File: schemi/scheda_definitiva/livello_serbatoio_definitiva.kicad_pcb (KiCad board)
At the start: 2 copper layers, 83 x 72 mm, 36 parts, among them J1 USB_B, J2 CONN_US, J3 CONN_LCD, J4 BTN_LED_GROUP, J5 ICSP, SW1 SW_RST, U1 FT232RL, U2 ATmega328P-PU, Y1 16MHz

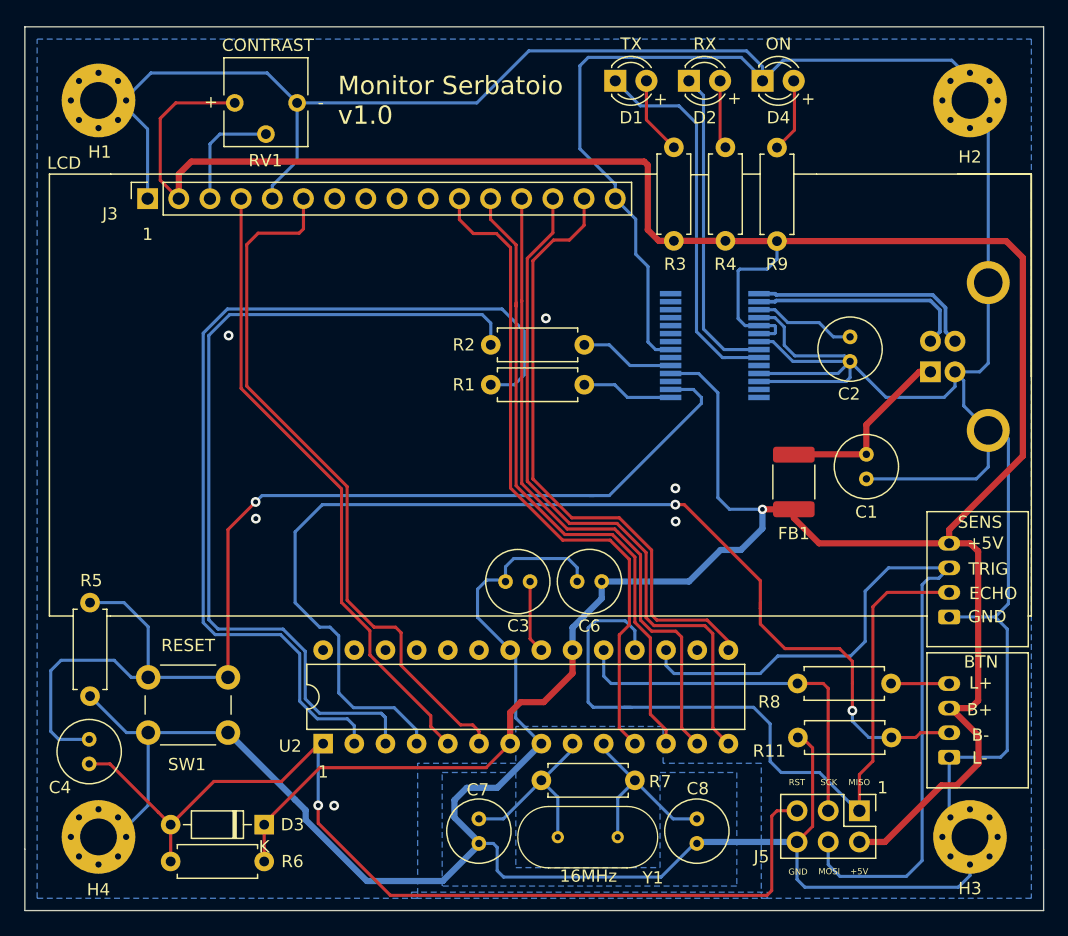
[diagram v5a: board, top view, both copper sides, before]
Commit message: fix a scheda - corrette footprint (adeguate a componenti in possesso) - nuovo routing e layout scheda - aggiunto logo - aggiornato gerber
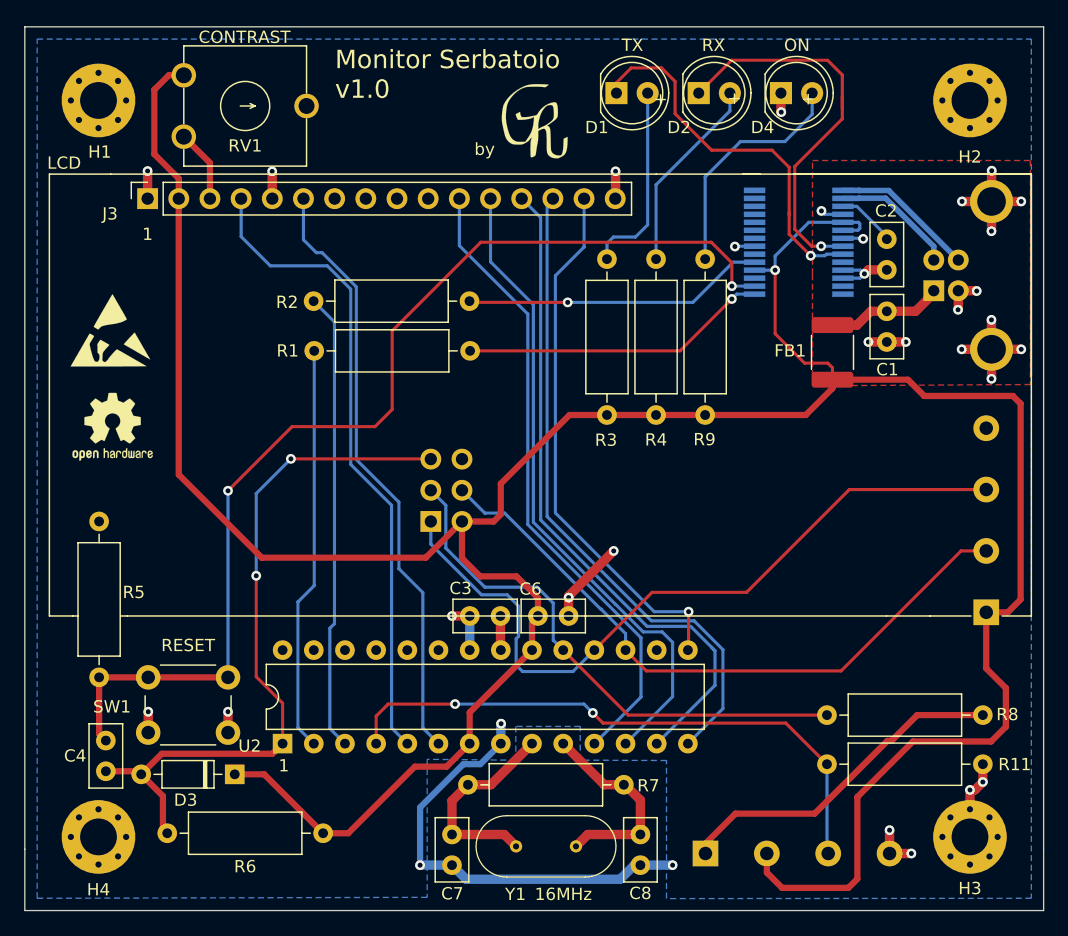
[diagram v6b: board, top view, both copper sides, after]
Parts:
- added G***: LOGO, simboli_custom:logo, F.Cu at (128.5, 75.7)
- added REF**: OSHW-Logo2_7.3x6mm_SilkScreen, Symbol:OSHW-Logo2_7.3x6mm_SilkScreen, F.Cu at (94.2, 100.6)
- added REF**: ESD-Logo_6.6x6mm_SilkScreen, Symbol:ESD-Logo_6.6x6mm_SilkScreen, F.Cu at (94.0, 92.7)
- C1, C2, C3, C4, C6, C7, C8: footprint Capacitor_THT:C_Radial_D5.0mm_H5.0mm_P2.00mm -> Capacitor_THT:C_Disc_D5.0mm_W2.5mm_P2.50mm
- D1, D2, D4: footprint LED_THT:LED_D3.0mm -> LED_THT:LED_D5.0mm
- J2: value CONN_US -> BTN_LED_GROUP; footprint Connector_Molex:Molex_Micro-Latch_53254-0470_1x04_P2.00mm_Horizontal -> simboli_custom:TerminalBlock_RND_205-00047_1x04_P5.00mm_Horizontal
- J4: value BTN_LED_GROUP -> CONN_US; footprint Connector_Molex:Molex_Micro-Latch_53254-0470_1x04_P2.00mm_Horizontal -> simboli_custom:TerminalBlock_RND_205-00047_1x04_P5.00mm_Horizontal
- J5: moved to B.Cu
- R1, R11, R2, R3, R4, R5, R6, R7, R9: footprint Resistor_THT:R_Axial_DIN0207_L6.3mm_D2.5mm_P7.62mm_Horizontal -> Resistor_THT:R_Axial_DIN0309_L9.0mm_D3.2mm_P12.70mm_Horizontal
- R8: value 390 -> 330; footprint Resistor_THT:R_Axial_DIN0207_L6.3mm_D2.5mm_P7.62mm_Horizontal -> Resistor_THT:R_Axial_DIN0309_L9.0mm_D3.2mm_P12.70mm_Horizontal
- RV1: footprint Potentiometer_THT:Potentiometer_Vishay_T73YP_Vertical -> simboli_custom:Trimmer_ACP_470
- SW1: footprint Button_Switch_THT:SW_PUSH_6mm -> Button_Switch_THT:SW_PUSH_6mm_H5mm
- moved J5 42.1 mm to (120.1, 108.3), turned to 0 degrees
- moved J2 27.7 mm to (142.4, 135.3), turned to 0 degrees
- moved R4 15.3 mm to (138.4, 99.6)
- moved R3 15.2 mm to (134.4, 99.6)
- moved R2 14.9 mm to (110.5, 90.3)
- moved R1 14.6 mm to (110.6, 94.4)
- moved J4 12.2 mm to (165.3, 115.7)
- moved C1 11.8 mm to (157.2, 91.2)
- moved FB1 11.0 mm to (152.8, 94.5)
- moved U1 10.8 mm to (150.1, 85.5)
- moved R9 10.8 mm to (142.4, 86.9)
- moved C2 8.50 mm to (157.2, 85.3)
- moved J1 6.62 mm to (161.1, 89.5)
- moved R5 6.13 mm to (93.0, 121.0), turned to 90 degrees
- moved R7 5.99 mm to (123.1, 129.8)
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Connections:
- C1 pad 2: BLK -> GND
- C2 pad 2: BLK -> GND
- C3 pad 2: BLK -> GND
- C6 pad 2: BLK -> GND
- C7 pad 1: BLK -> GND
- C8 pad 1: BLK -> GND
- D4 pad 1: BLK -> GND
- H1 pad 1: BLK -> GND
- H2 pad 1: BLK -> GND
- H3 pad 1: BLK -> GND
- H4 pad 1: BLK -> GND
- J1 pad 4: BLK -> GND
- J1 pad 5: BLK -> GND
- J2 pad 1: BLK -> Net-(J2-Pad1)
- J2 pad 2: D12 -> VDD
- J2 pad 3: D11 -> D2
- J2 pad 4: VDD -> GND
- J3 pad 1: BLK -> GND
- J3 pad 16: BLK -> GND
- J3 pad 5: BLK -> GND
- J4 pad 1: BLK -> VDD
- J4 pad 2: D2 -> D11
- J4 pad 3: VDD -> D12
- J4 pad 4: Net-(J4-Pad4) -> GND
- J5 pad 6: BLK -> GND
- R11 pad 2: BLK -> GND
- R5 pad 2: BLK -> GND
- R8 pad 2: Net-(J4-Pad4) -> Net-(J2-Pad1)
- RV1 pad 3: BLK -> GND
- SW1 pad 2: BLK -> GND
- U1 pad 18: BLK -> GND
- U1 pad 21: BLK -> GND
- U1 pad 25: BLK -> GND
- U1 pad 26: BLK -> GND
- U1 pad 7: BLK -> GND
- U2 pad 22: BLK -> GND
- U2 pad 8: BLK -> GND
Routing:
- net BLK: track 425.6 -> 0.00 mm, vias 6 -> 0
- net GND: track 0.00 -> 106.1 mm, vias 0 -> 32
- net TX: track 77.4 -> 33.1 mm
- net D2: track 91.4 -> 48.9 mm
- net RX: track 71.5 -> 37.4 mm
- net Net-(J2-Pad1): track 0.00 -> 27.7 mm
- net ICSP_RST: track 81.3 -> 57.9 mm, vias 1 -> 2
- net Net-(R1-Pad2): track 7.46 -> 25.1 mm, vias 0 -> 1
- net Net-(R2-Pad2): track 7.73 -> 24.6 mm, vias 0 -> 1
- net Net-(D4-Pad2): track 6.05 -> 19.3 mm
- net D13: track 30.8 -> 43.7 mm
- net D11: track 66.2 -> 53.6 mm
- net VDD: track 260.1 -> 248.8 mm
- net Net-(D2-Pad2): track 5.60 -> 16.0 mm
- net Net-(D1-Pad2): track 6.34 -> 16.0 mm
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- added copper zone on B.Cu, net GND
- added copper zone on F.Cu, net GND
- removed copper zone on B.Cu, net BLK
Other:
- board text added: "E"
- board text added: "T"
- board text added: "W: 17.7 mils / D: 7 mils / PCB thickness: 0.6 mm 2-layer FR-4 Zdiff: 102ohm (in range 90ohm +-15%) Zcomm: 52.5 ohm (leggermente fuori range 45ohm +- 15%)"
- board text added: "by"
- board text removed: "-"
- board text removed: "ECHO"
- board text removed: "TRIG"

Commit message: aggiunta protezione ESD - nuovo routing usb - nuove immagini pcb
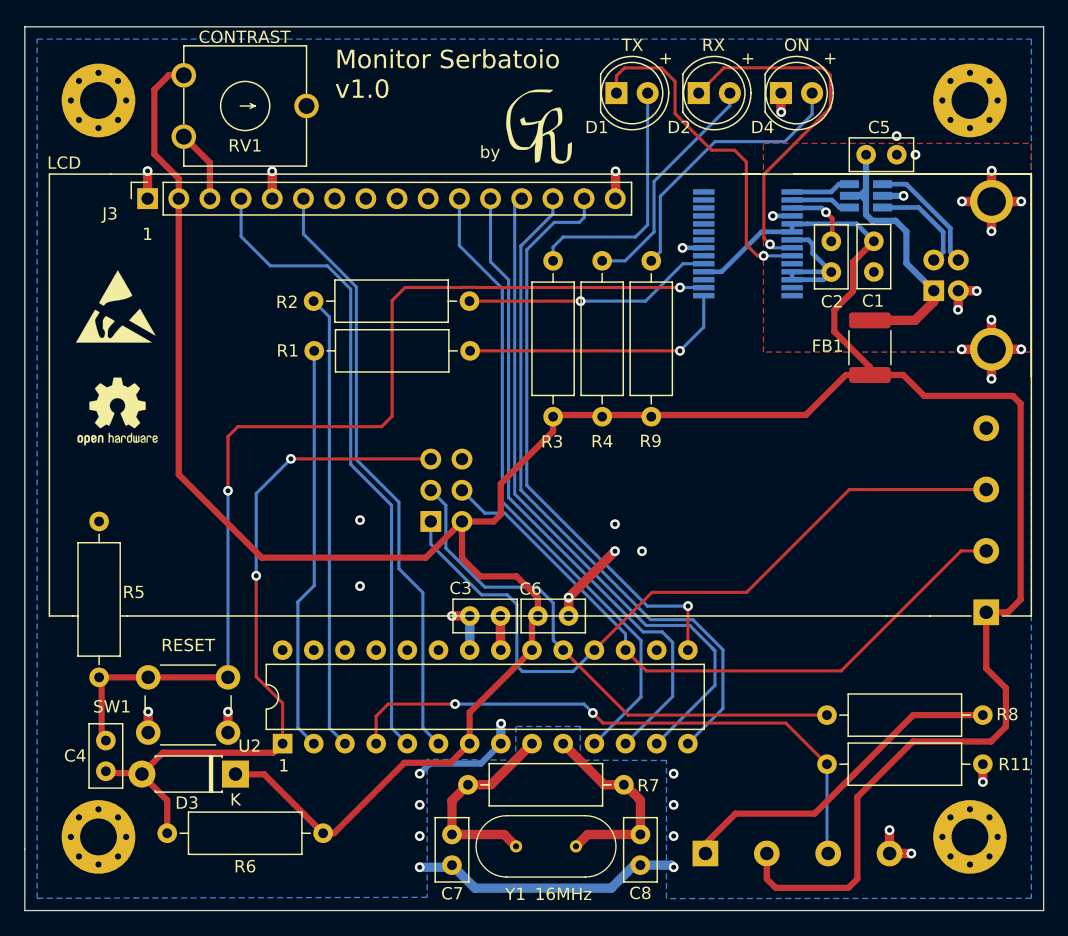
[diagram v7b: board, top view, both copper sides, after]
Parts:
- added C5: 100nF, Capacitor_THT:C_Disc_D5.0mm_W2.5mm_P2.50mm, F.Cu at (158.0, 78.4)
- added U3: USBLC6-2SC6, Package_TO_SOT_SMD:SOT-23-6_Handsoldering, B.Cu at (155.5, 81.8)
- D3: value 1N4148TR -> 1N4700; footprint Diode_THT:D_DO-35_SOD27_P7.62mm_Horizontal -> Diode_THT:D_DO-41_SOD81_P7.62mm_Horizontal
- moved C2 4.53 mm to (152.7, 85.5)
- moved R3 4.39 mm to (130.0, 99.8)
- moved R4 4.39 mm to (134.0, 99.8)
- moved R9 4.39 mm to (138.0, 87.1)
- moved U1 4.14 mm to (145.9, 85.7)
- moved C1 3.37 mm to (156.2, 88.0), turned to 90 degrees
- moved FB1 3.07 mm to (155.8, 94.1)
- moved REF** 1.99 mm to (94.4, 90.8)
- moved REF** 1.31 mm to (94.5, 99.3)
- moved G*** 0.56 mm to (128.9, 76.1)
- moved D3 0.06 mm to (104.2, 128.9)
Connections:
- C1 pad 1: Net-(C1-Pad1) -> GND
- C1 pad 2: GND -> VDD
- FB1 pad 2: Net-(C1-Pad1) -> VBUS
- J1 pad 1: Net-(C1-Pad1) -> VBUS
- J1 pad 2: /D- -> D_IN_-
- J1 pad 3: /D+ -> D_IN_+
- U1 pad 15: /D+ -> D_OUT_+
- U1 pad 16: /D- -> D_OUT_-
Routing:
- net VBUS: track 0.00 -> 23.3 mm
- net /D+: track 11.8 -> 0.00 mm
- net /D-: track 10.1 -> 0.00 mm
- net D_IN_+: track 0.00 -> 9.87 mm
- net Net-(C1-Pad1): track 9.53 -> 0.00 mm
- net D_IN_-: track 0.00 -> 8.44 mm
- net VDD: track 248.8 -> 256.0 mm, vias 1 -> 0
- net GND: track 106.1 -> 99.1 mm, vias 32 -> 40
- net D_OUT_+: track 0.00 -> 4.93 mm
- net D_OUT_-: track 0.00 -> 4.92 mm
- net Net-(D1-Pad2): track 16.0 -> 20.3 mm
- net Net-(R2-Pad2): track 24.6 -> 20.3 mm
- net DTR: track 88.7 -> 84.8 mm
- net BLA: track 43.9 -> 47.3 mm
- net Net-(D1-Pad1): track 31.1 -> 27.8 mm
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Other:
- board text removed: "W: 17.7 mils / D: 7 mils / PCB thickness: 0.6 mm 2-layer FR-4 Zdiff: 102ohm (in range 90ohm +-15%) Zcomm: 52.5 ohm (leggermente fuori range 45ohm +- 15%)"

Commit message: allineamento modello 3d + fix minori pcb - aggiornato modello box - aggiunto logo a box - nuovi modelli 3d fusibile e trimmer - aggiornato sch per fusibile - aggiornato pcb - nuove immagini + doc prototipo pdf
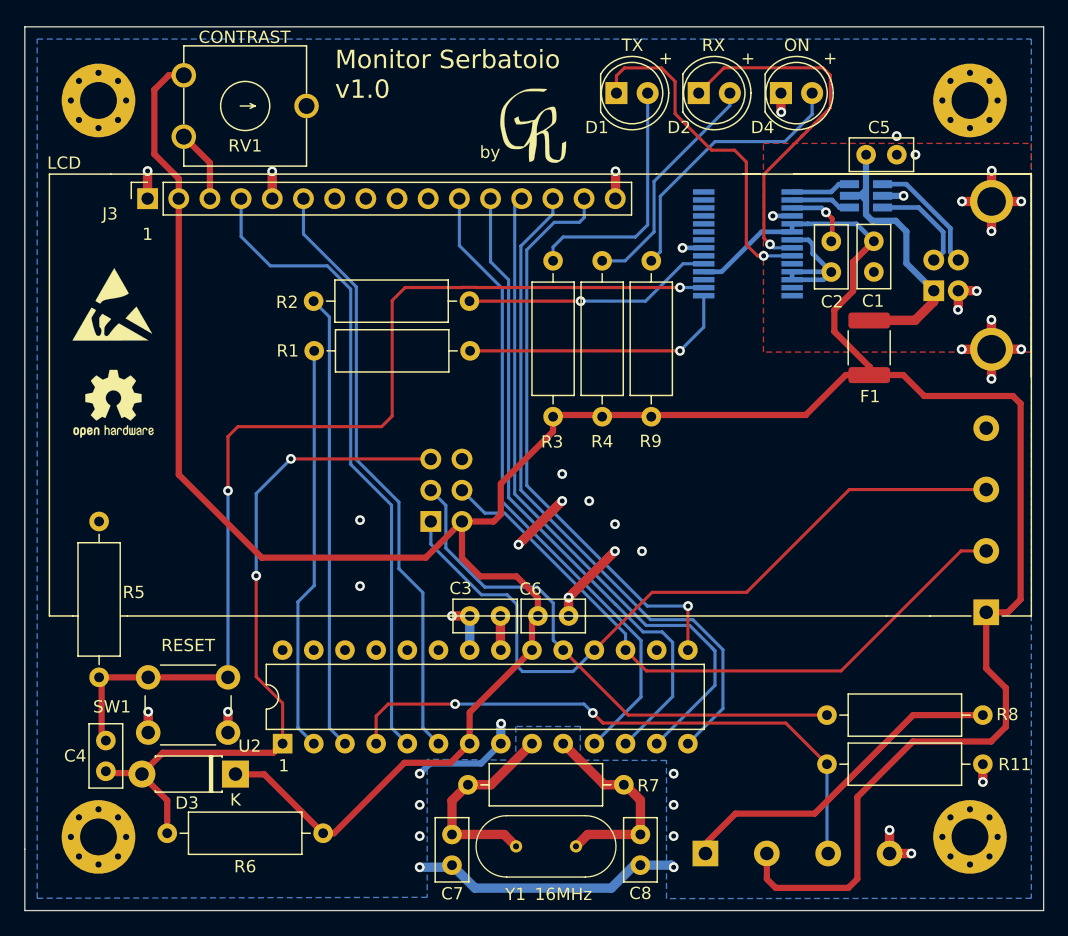
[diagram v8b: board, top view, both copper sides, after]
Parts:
- removed FB1: MF-MSMF050-2, Inductor_SMD:L_1812_4532Metric_Pad1.30x3.40mm_HandSolder
- added F1: MF-MSMF050-2, simboli_custom:MF-MSMF_1812_4532Metric_Pad1.30x3.40mm_HandSolder, F.Cu at (155.8, 94.2)
- moved REF** 0.71 mm to (94.2, 98.7)
- moved G*** 0.49 mm to (128.4, 76.1)
- moved REF** 0.34 mm to (94.1, 90.6)
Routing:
- net GND: track 99.1 -> 104.1 mm, vias 40 -> 44
